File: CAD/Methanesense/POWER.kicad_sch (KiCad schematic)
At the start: 22 parts, among them J1 USB_C_Receptacle_USB2.0_14P, SW3 KMR223GLFG, U1 AP63205WU, U3 nPM1300-QEXX, U4 AP131-20, U7 FT230XQ

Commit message: WIP
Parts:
- removed C1: 10uF, Capacitor_SMD:C_0805_2012Metric, symbol Library:C
- removed C2: 0.1uF, Capacitor_SMD:C_0402_1005Metric, symbol Library:C
- removed C4, C5: 22uf, Capacitor_SMD:C_0402_1005Metric, symbol Library:C
- removed D4, D7, D8: 1N5819WS, Diode_SMD:D_SOD-323, symbol Library:1N4148WS
- removed L1: 6.8uH, Inductor_SMD:L_1008_2520Metric, symbol Device:L
- removed U1: AP63205WU, Package_TO_SOT_SMD:TSOT-23-6, symbol Regulator_Switching:AP63201WU
- added BT1: 1042P, Battery:BatteryHolder_MPD_BH-18650-PC2, symbol Device:Battery_Cell
- added BT2: 18650-3500mAH, symbol Device:Battery_Cell
- added C10, C12, C37: 10uF, Capacitor_SMD:C_0805_2012Metric, symbol Library:C
- added C11: 1uF, Capacitor_SMD:C_0603_1608Metric, symbol Library:C
- added F1: 0805L110WR, Resistor_SMD:R_1206_3216Metric, symbol Device:Polyfuse
- added L3: 2.2uH, Inductor_SMD:L_1008_2520Metric, symbol Device:L
- added NT1: NetTie_2, esprelay:Viatie, symbol Device:NetTie_2
- added R1: 68k, Resistor_SMD:R_0603_1608Metric, symbol Library:R
- added TH1: 10k NTC, Resistor_SMD:R_0603_1608Metric, symbol Device:Thermistor_NTC
- C3, C6, C7, C8, C9: footprint Capacitor_SMD:C_0402_1005Metric -> Capacitor_SMD:C_0603_1608Metric
- D10, D11, D9: footprint (none) -> LED_SMD:LED_0603_1608Metric
- J1: footprint (none) -> Methanesense:USB_C_Receptacle_HCTL_HC-TYPE-C-16P-01A
- U4: value AP131-20 -> AP7331-20WG-7
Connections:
- net +5V: now also D10.2 (A), D11.2 (A), D9.2 (A), U3.22 (VBUSOUT), C11.1; no longer U3.21 (VBUS)
- net +BATT: now also F1.1
- net GND: now also U3.16 (VSET2), U3.29 (LSOUT1/VOUTLDO1), U3.31 (LSOUT2/VOUTLDO2), U3.6 (PVSS2), BT1.2 (-), BT2.2 (-), C11.2, C12.2, C37.2, NT1.2, R1.2, TH1.1
- net TXD: now reaches U7.15 (TXD)
- net ~{RTS}: now reaches U7.16 (~{RTS})
- net RXD: now reaches U7.2 (RXD)
- net ~{CTS}: now reaches U7.4 (~{CTS})
- net +2V0: now reaches U3.1 (VOUT1)
- net +2V0: now also U3.12 (VDDIO), U3.28 (LSIN1/VINLDO1), U3.30 (LSIN2/VINLDO2), C10.1, L3.1
- net SDA: now reaches U3.13 (SDA)
- net SCL: now reaches U3.14 (SCL)
- net at U3.17 (VSET1): now also R1.1
- net at U3.18 (NTC): now also TH1.2
- net PVSS1: now reaches U3.2 (PVSS1)
- net PVSS1: now also C10.2, NT1.1
- net VSYS: now reaches U3.20 (VSYS)
- net VSYS: now also U3.4 (PVDD), C12.1, C37.1
- net SW1: now reaches U3.3 (SW1)
- net SW1: now also L3.2
- net VCC: now reaches U3.32 (VOUT2)
- net +5P renamed +5VL
- net +5VL: now also U3.21 (VBUS)
- new net: BT1.1 (+), BT2.1 (+), F1.2
- no-connect marks 6 -> 10
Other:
- note added: "18650"
- note added: "PMIC"
- note added: "USB"
- note removed: "HIGH_VOLTAGE_REGULATOR"
- moved on the sheet: C3, C6, C7, C8, C9, D10, D11, D9, J1, SW3, U3, U4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

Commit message: WIP
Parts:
- removed NT1: NetTie_2, esprelay:Viatie, symbol Device:NetTie_2
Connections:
- net PVSS1 is gone; now on net GND: C10.2, U3.2 (PVSS1)
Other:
- note added: "Connect with single via"
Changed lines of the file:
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@@
 	(wire
 		(pts
+			(xy 264.16 97.79) (xy 259.08 97.79)
+		)
+		(stroke
+			(width 0)
+			(type default)
+		)
+	)
+	(wire
+		(pts
 			(xy 81.28 90.17) (xy 81.28 87.63)
 		)
@@
 		)
 	)
+	(text "Connect with single via\n"
+		(exclude_from_sim no)
+		(at 261.62 96.774 0)
+		(effects
+			(font
+				(size 1.27 1.27)
+			)
+		)
+	)
 	(text "USB\n"
 		(exclude_from_sim no)
@@
 		)
 		(instances
-			(project ""
+			(project "Methanesense"
 				(path "/51bbc301-ea4a-44e0-84a7-cf42c64443ca/29268011-ceb4-4614-83a3-b1b699d92774"
 					(reference "#PWR028")
@@
 		)
 		(instances
-			(project ""
+			(project "Methanesense"
 				(path "/51bbc301-ea4a-44e0-84a7-cf42c64443ca/29268011-ceb4-4614-83a3-b1b699d92774"
 					(reference "U7")
@@
 		)
 		(instances
-			(project ""
+			(project "Methanesense"
 				(path "/51bbc301-ea4a-44e0-84a7-cf42c64443ca/29268011-ceb4-4614-83a3-b1b699d92774"
 					(reference "TH1")
@@
 		)
 		(instances
-			(project ""
+			(project "Methanesense"
 				(path "/51bbc301-ea4a-44e0-84a7-cf42c64443ca/29268011-ceb4-4614-83a3-b1b699d92774"
 					(reference "U4")
@@
 	)
 	(symbol
-		(lib_id "Device:NetTie_2")
-		(at 262.89 97.79 0)
-		(mirror x)
-		(unit 1)
-		(exclude_from_sim no)
-		(in_bom no)
-		(on_board yes)
-		(dnp no)
-		(property "Reference" "NT1"
-			(at 262.89 92.71 0)
-			(effects
-				(font
-					(size 1.27 1.27)
-				)
-			)
-		)
-		(property "Value" "NetTie_2"
-			(at 262.89 95.25 0)
-			(effects
-				(font
-					(size 1.27 1.27)
-				)
-			)
-		)
-		(property "Footprint" "esprelay:Viatie"
-			(at 262.89 97.79 0)
-			(effects
-				(font
-					(size 1.27 1.27)
-				)
-				(hide yes)
-			)
-		)
-		(property "Datasheet" "~"
-			(at 262.89 97.79 0)
-			(effects
-				(font
-					(size 1.27 1.27)
-				)
-				(hide yes)
-			)
-		)
-		(property "Description" "Net tie, 2 pins"
-			(at 262.89 97.79 0)
-			(effects
-				(font
-					(size 1.27 1.27)
-				)
-				(hide yes)
-			)
-		)
-		(property "TEST" ""
-			(at 262.89 97.79 0)
-			(effects
-				(font
-					(size 1.27 1.27)
-				)
-			)
-		)
-		(pin "2"
-		)
-		(pin "1"
-		)
-		(instances
-			(project ""
-				(path "/51bbc301-ea4a-44e0-84a7-cf42c64443ca/29268011-ceb4-4614-83a3-b1b699d92774"
-					(reference "NT1")
-					(unit 1)
-				)
-			)
-		)
-	)
-	(symbol
 		(lib_id "power:+5VL")
 		(at 107.95 110.49 0)
@@
 	(symbol
 		(lib_id "power:GND")
-		(at 265.43 97.79 0)
+		(at 264.16 97.79 0)
 		(unit 1)
 		(exclude_from_sim no)
@@
 		(dnp no)
 		(property "Reference" "#PWR046"
-			(at 265.43 104.14 0)
+			(at 264.16 104.14 0)
 			(effects
 				(font
@@
 		)
 		(property "Value" "GND"
-			(at 265.176 103.124 90)
+			(at 264.414 101.6 0)
 			(effects
 				(font
@@
 		)
 		(property "Footprint" ""
-			(at 265.43 97.79 0)
+			(at 264.16 97.79 0)
 			(effects
 				(font
@@
 		)
 		(property "Datasheet" ""
-			(at 265.43 97.79 0)
+			(at 264.16 97.79 0)
 			(effects
 				(font
@@
 		)
 		(property "Description" ""
-			(at 265.43 97.79 0)
+			(at 264.16 97.79 0)
 			(effects
 				(font
@@
 		)
 		(instances
-			(project ""
+			(project "Methanesense"
 				(path "/51bbc301-ea4a-44e0-84a7-cf42c64443ca/29268011-ceb4-4614-83a3-b1b699d92774"
 					(reference "#PWR027")
@@
 		)
 		(instances
-			(project ""
+			(project "Methanesense"
 				(path "/51bbc301-ea4a-44e0-84a7-cf42c64443ca/29268011-ceb4-4614-83a3-b1b699d92774"
 					(reference "J1")
@@
 	(symbol
 		(lib_id "power:GND")
-		(at 260.35 97.79 0)
+		(at 259.08 97.79 0)
 		(unit 1)
 		(exclude_from_sim no)
@@
 		(dnp no)
 		(property "Reference" "#PWR045"
-			(at 260.35 104.14 0)
+			(at 259.08 104.14 0)
 			(effects
 				(font
@@
 		)
 		(property "Value" "PVSS1"
-			(at 260.35 101.6 0)
+			(at 259.08 101.6 0)
 			(effects
 				(font
@@
 		)
 		(property "Footprint" ""
-			(at 260.35 97.79 0)
+			(at 259.08 97.79 0)
 			(effects
 				(font
@@
 		)
 		(property "Datasheet" ""
-			(at 260.35 97.79 0)
+			(at 259.08 97.79 0)
 			(effects
 				(font
@@
 		)
 		(property "Description" ""
-			(at 260.35 97.79 0)
+			(at 259.08 97.79 0)
 			(effects
 				(font
@@
 		)
 		(property "TEST" ""
-			(at 260.35 97.79 0)
+			(at 259.08 97.79 0)
 			(effects
 				(font
@@
 		)
 		(instances
-			(project ""
+			(project "Methanesense"
 				(path "/51bbc301-ea4a-44e0-84a7-cf42c64443ca/29268011-ceb4-4614-83a3-b1b699d92774"
 					(reference "U3")
@@
 		)
 		(instances
-			(project ""
+			(project "Methanesense"
 				(path "/51bbc301-ea4a-44e0-84a7-cf42c64443ca/29268011-ceb4-4614-83a3-b1b699d92774"
 					(reference "#PWR053")

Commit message: Allmost there
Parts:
- added R4, R5: 0R, Resistor_SMD:R_0603_1608Metric, symbol Library:R
- BT1: value 1042P -> BH-18650-PC2; footprint Battery:BatteryHolder_MPD_BH-18650-PC2 -> Methanesense:BatteryHolder_MPD_BH-18650-PC2
- renumbered BT2 to BAT1
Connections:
- net +2V0: now also R4.1; no longer U3.28 (LSIN1/VINLDO1)
- net GND: no longer U3.31 (LSOUT2/VOUTLDO2)
- net VCCIOUSB: now reaches C7.1, U4.5 (OUT), U7.1 (VCCIO)
- net VCCIOUSB: now also R5.2
- net USBDP: now reaches C6.2, J1.A6 (D+), J1.B6 (D+), U7.6 (USBDP)
- net USBDN: now reaches C3.2, J1.A7 (D-), J1.B7 (D-), U7.7 (USBDM)
- new net +2V0SW: R4.2, U3.31 (LSOUT2/VOUTLDO2)
- new net USB_DET: R5.1
- no-connect marks 10 -> 11
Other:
- note added: "Addr: 110 1011"
- moved on the sheet: BAT1

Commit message: WIP
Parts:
- SW3: MPN (none) -> KMR223GLFG
- TH1: MPN (none) -> 10k NTC
- U3: MPN (none) -> nPM1300-QEAA
- U4: MPN (none) -> AP7331-20WG-7
- U7: MPN (none) -> FT230XQ
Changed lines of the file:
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@@
 			)
 		)
+		(property "MPN" "FT230XQ"
+			(at 110.49 128.27 0)
+			(effects
+				(font
+					(size 1.27 1.27)
+				)
+				(hide yes)
+			)
+		)
 		(pin "3"
 		)
@@
 			)
 		)
+		(property "MPN" ""
+			(at 256.54 82.55 0)
+			(effects
+				(font
+					(size 1.27 1.27)
+				)
+				(hide yes)
+			)
+		)
 		(pin "1"
 		)
@@
 			)
 		)
+		(property "MPN" "10k NTC"
+			(at 246.38 127 0)
+			(effects
+				(font
+					(size 1.27 1.27)
+				)
+				(hide yes)
+			)
+		)
 		(pin "1"
 		)
@@
 			)
 		)
+		(property "MPN" ""
+			(at 161.29 119.38 0)
+			(effects
+				(font
+					(size 1.27 1.27)
+				)
+				(hide yes)
+			)
+		)
 		(pin "1"
 		)
@@
 			)
 		)
+		(property "MPN" "AP7331-20WG-7"
+			(at 88.9 90.17 0)
+			(effects
+				(font
+					(size 1.27 1.27)
+				)
+				(hide yes)
+			)
+		)
 		(pin "5"
 		)
@@
 			)
 		)
+		(property "MPN" ""
+			(at 99.06 93.98 0)
+			(effects
+				(font
+					(size 1.27 1.27)
+				)
+				(hide yes)
+			)
+		)
 		(pin "1"
 		)
@@
 			)
 		)
+		(property "MPN" ""
+			(at 246.38 82.55 0)
+			(effects
+				(font
+					(size 1.27 1.27)
+				)
+				(hide yes)
+			)
+		)
 		(pin "1"
 		)
@@
 			)
 		)
+		(property "MPN" "KMR223GLFG"
+			(at 160.02 127 0)
+			(effects
+				(font
+					(size 1.27 1.27)
+				)
+				(hide yes)
+			)
+		)
 		(pin "2"
 		)
@@
 			)
 		)
+		(property "MPN" ""
+			(at 71.12 181.61 0)
+			(effects
+				(font
+					(size 1.27 1.27)
+				)
+				(hide yes)
+			)
+		)
 		(pin "1"
 		)
@@
 			)
 		)
+		(property "MPN" ""
+			(at 240.03 52.07 0)
+			(effects
+				(font
+					(size 1.27 1.27)
+				)
+				(hide yes)
+			)
+		)
 		(pin "1"
 		)
@@
 			)
 		)
+		(property "MPN" ""
+			(at 50.8 125.73 0)
+			(effects
+				(font
+					(size 1.27 1.27)
+				)
+				(hide yes)
+			)
+		)
 		(pin "A12"
 		)
@@
 			)
 		)
+		(property "MPN" ""
+			(at 106.68 93.98 0)
+			(effects
+				(font
+					(size 1.27 1.27)
+				)
+				(hide yes)
+			)
+		)
 		(pin "1"
 		)
@@
 			)
 		)
+		(property "MPN" ""
+			(at 77.47 135.89 0)
+			(effects
+				(font
+					(size 1.27 1.27)
+				)
+				(hide yes)
+			)
+		)
 		(pin "1"
 		)
@@
 			)
 		)
+		(property "MPN" ""
+			(at 77.47 93.98 0)
+			(effects
+				(font
+					(size 1.27 1.27)
+				)
+				(hide yes)
+			)
+		)
 		(pin "1"
 		)
@@
 			)
 		)
+		(property "MPN" ""
+			(at 227.33 52.07 0)
+			(effects
+				(font
+					(size 1.27 1.27)
+				)
+				(hide yes)
+			)
+		)
 		(pin "1"
 		)
@@
 			)
 		)
+		(property "MPN" ""
+			(at 262.89 114.3 0)
+			(effects
+				(font
+					(size 1.27 1.27)
+				)
+				(hide yes)
+			)
+		)
 		(pin "1"
 		)
@@
 			)
 		)
+		(property "MPN" ""
+			(at 161.29 88.9 0)
+			(effects
+				(font
+					(size 1.27 1.27)
+				)
+				(hide yes)
+			)
+		)
 		(pin "2"
 		)
@@
 			)
 		)
+		(property "MPN" ""
+			(at 116.84 87.63 0)
+			(effects
+				(font
+					(size 1.27 1.27)
+				)
+				(hide yes)
+			)
+		)
 		(pin "1"
 		)
@@
 			)
 		)
+		(property "MPN" ""
+			(at 161.29 86.36 0)
+			(effects
+				(font
+					(size 1.27 1.27)
+				)
+				(hide yes)
+			)
+		)
 		(pin "2"
 		)
@@
 			)
 		)
+		(property "MPN" ""
+			(at 49.53 171.45 0)
+			(effects
+				(font
+					(size 1.27 1.27)
+				)
+				(hide yes)
+			)
+		)
 		(pin "1"
 		)
@@
 			)
 		)
+		(property "MPN" ""
+			(at 219.71 52.07 0)
+			(effects
+				(font
+					(size 1.27 1.27)
+				)
+				(hide yes)
+			)
+		)
 		(pin "1"
 		)
@@
 			)
 		)
+		(property "MPN" ""
+			(at 49.53 181.61 0)
+			(effects
+				(font
+					(size 1.27 1.27)
+				)
+				(hide yes)
+			)
+		)
 		(pin "1"
 		)
@@
 			)
 		)
+		(property "MPN" ""
+			(at 69.85 135.89 0)
+			(effects
+				(font
+					(size 1.27 1.27)
+				)
+				(hide yes)
+			)
+		)
 		(pin "1"
 		)
@@
 			)
 		)
+		(property "MPN" ""
+			(at 161.29 91.44 0)
+			(effects
+				(font
+					(size 1.27 1.27)
+				)
+				(hide yes)
+			)
+		)
 		(pin "2"
 		)
@@
 			)
 		)
+		(property "MPN" "nPM1300-QEAA"
+			(at 204.47 99.06 0)
+			(effects
+				(font
+					(size 1.27 1.27)
+				)
+				(hide yes)
+			)
+		)

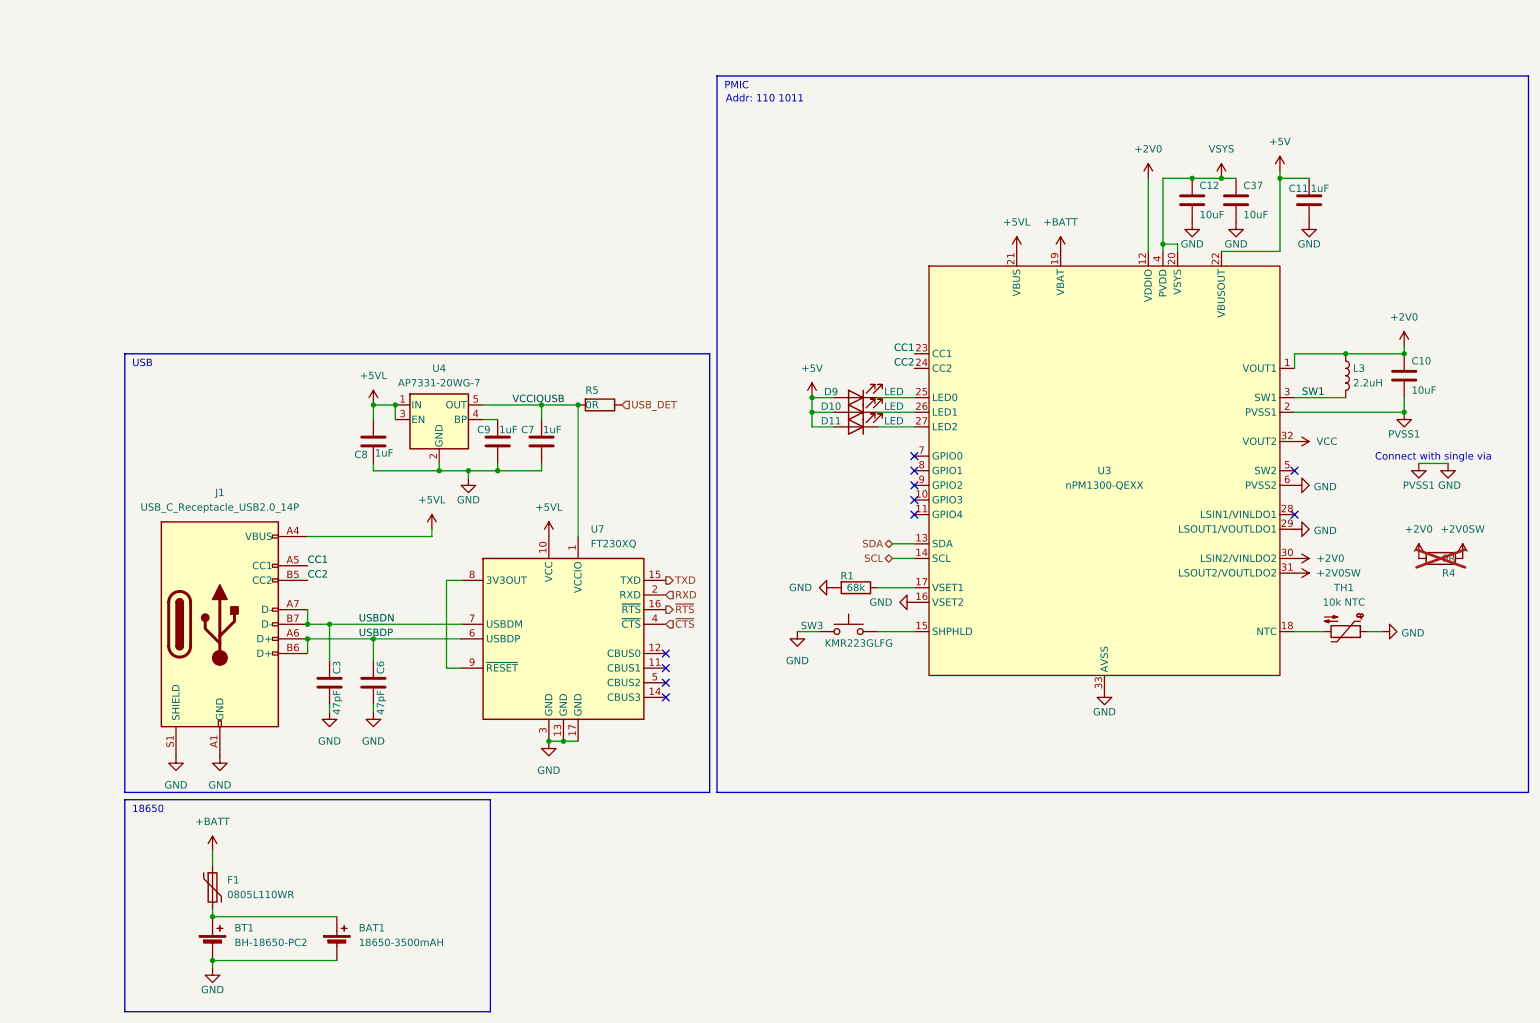
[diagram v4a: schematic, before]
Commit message: NRF footprint change
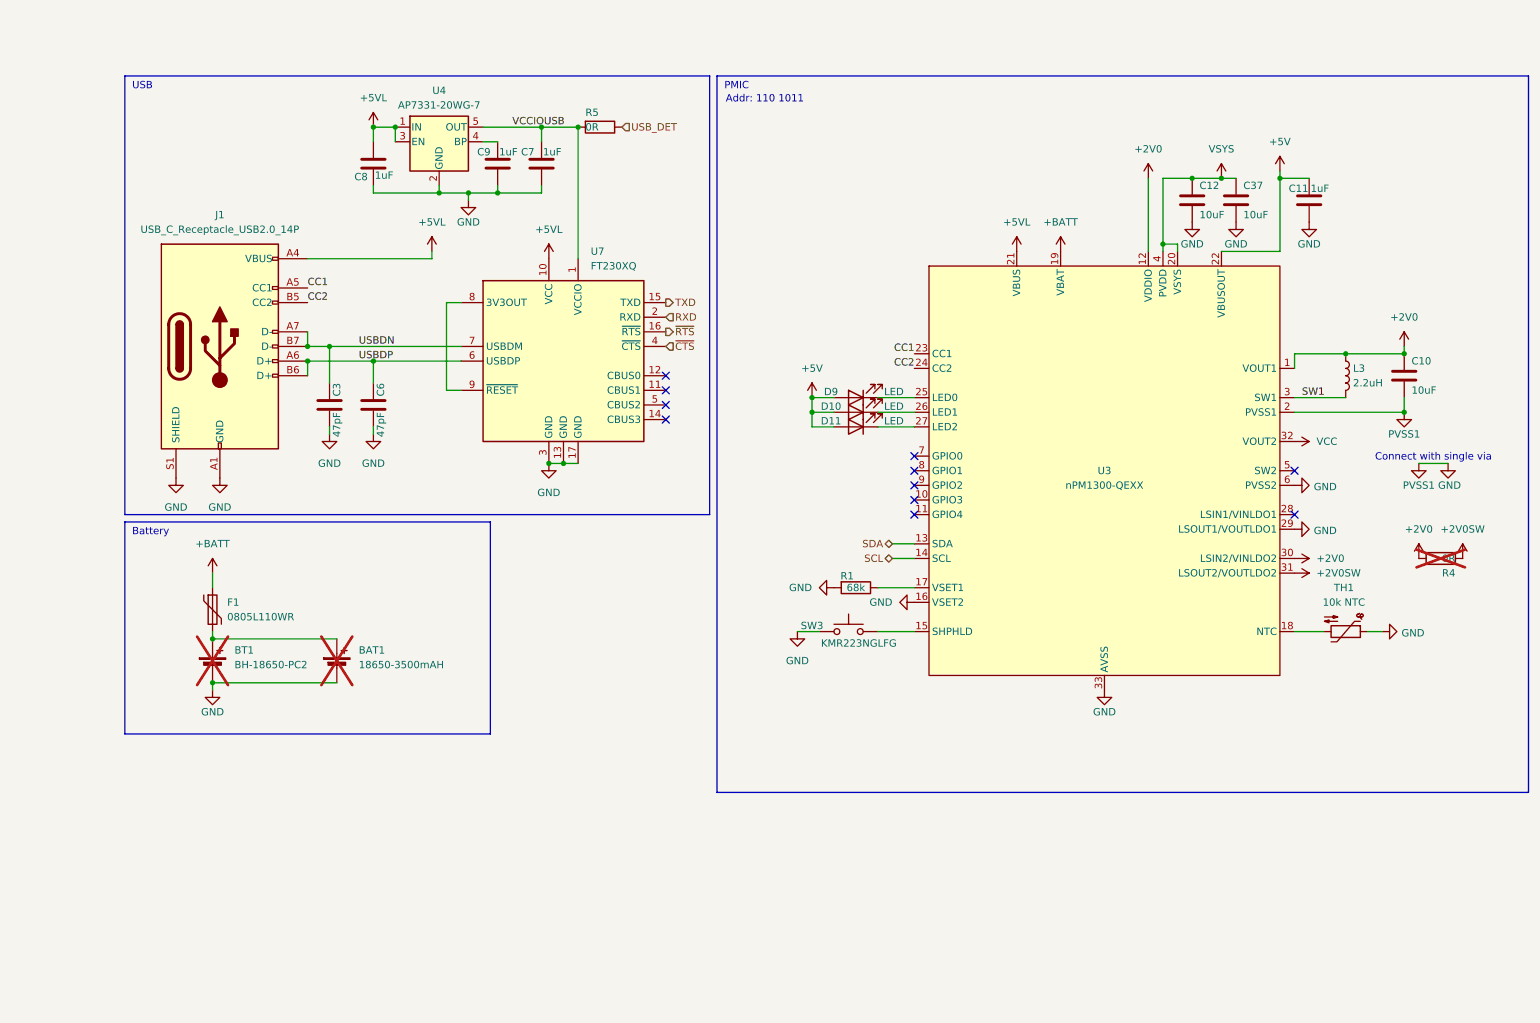
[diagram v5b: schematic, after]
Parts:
- BAT1: now not fitted
- BT1: MPN (none) -> BH-18650-PC2; now not fitted
- C10, C12, C37: LCSC Part # C415703 -> (none)
- C11, C3, C6, C7, C8, C9: LCSC Part # C307331 -> (none)
- D10, D11, D9: MPN (none) -> LG L29K-G2J1-24-Z
- F1: footprint Resistor_SMD:R_1206_3216Metric -> Fuse:Fuse_0805_2012Metric; MPN (none) -> 0805L110WR
- J1: MPN (none) -> 12402012E212A
- L3: MPN (none) -> CVH252009-2R2M
- R4, R5: LCSC Part # C25076 -> (none)
- SW3: value KMR223GLFG -> KMR223NGLFG; footprint Button_Switch_SMD:SW_Push_1P1T_NO_CK_KMR2 -> Methanesense:SW_Push_1P1T_NO_CK_KMR2; MPN KMR223GLFG -> KMR223NGLFG
- U3: footprint Package_DFN_QFN:QFN-32-1EP_5x5mm_P0.5mm_EP3.6x3.6mm -> Methanesense:QFN-32-1EP_5x5mm_P0.5mm_EP3.6x3.6mm; MPN nPM1300-QEAA -> nPM1300-QEAA-R7
- U7: footprint Package_DFN_QFN:QFN-16-1EP_4x4mm_P0.65mm_EP2.1x2.1mm -> Methanesense:QFN-16-1EP_4x4mm_P0.65mm_EP2.1x2.1mm
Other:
- note added: "Battery"
- note removed: "18650"
- moved on the sheet: C3, C6, C7, C8, C9, F1, J1, R5, U4, U7

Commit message: Rev 2.0.0
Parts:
- added C15: 4.7uF, Capacitor_SMD:C_0603_1608Metric, symbol Device:C
- added C16: 1uF, Capacitor_SMD:C_0603_1608Metric, symbol Library:C
- BT1: now fitted
- TH1: MPN 10k NTC -> NTCG163JF103FT1
- U3: footprint Methanesense:QFN-32-1EP_5x5mm_P0.5mm_EP3.6x3.6mm -> Methanesense:QFN-32-1EP_5x5mm_P0.5mm_EP3.6x3.6mm_ThermalVias
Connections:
- net VCC is gone; now on net VSYS: U3.32 (VOUT2)
- net +5V: no longer D10.2 (A), D11.2 (A), D9.2 (A)
- net +5VL: now also C16.1
- net +BATT: now also C15.1
- net GND: now also C15.2, C16.2
- net VSYS: now also D10.2 (A), D11.2 (A), D9.2 (A)
